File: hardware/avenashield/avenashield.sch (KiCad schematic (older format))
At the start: 4 parts, among them J3 CAN_TRA_HEADER, J4 CAN_IMP_HEADER, SW1 CAN 1 ON/OFF, SW2 CAN 2 ON/OFF

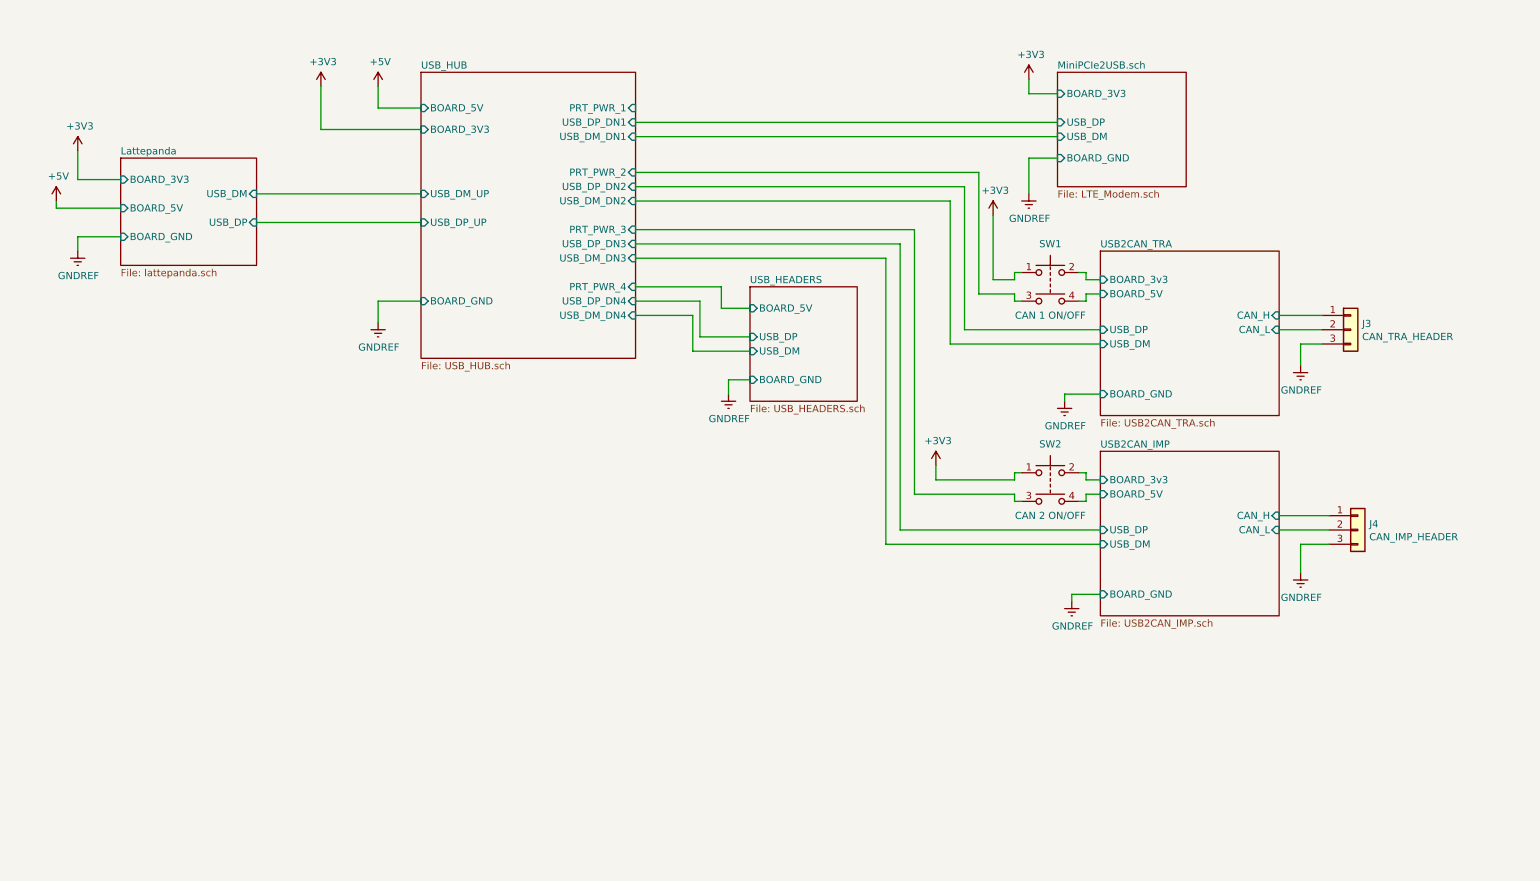
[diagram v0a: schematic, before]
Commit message: Added MiniPCIe latch clip and replaced onboard LEDs with connector
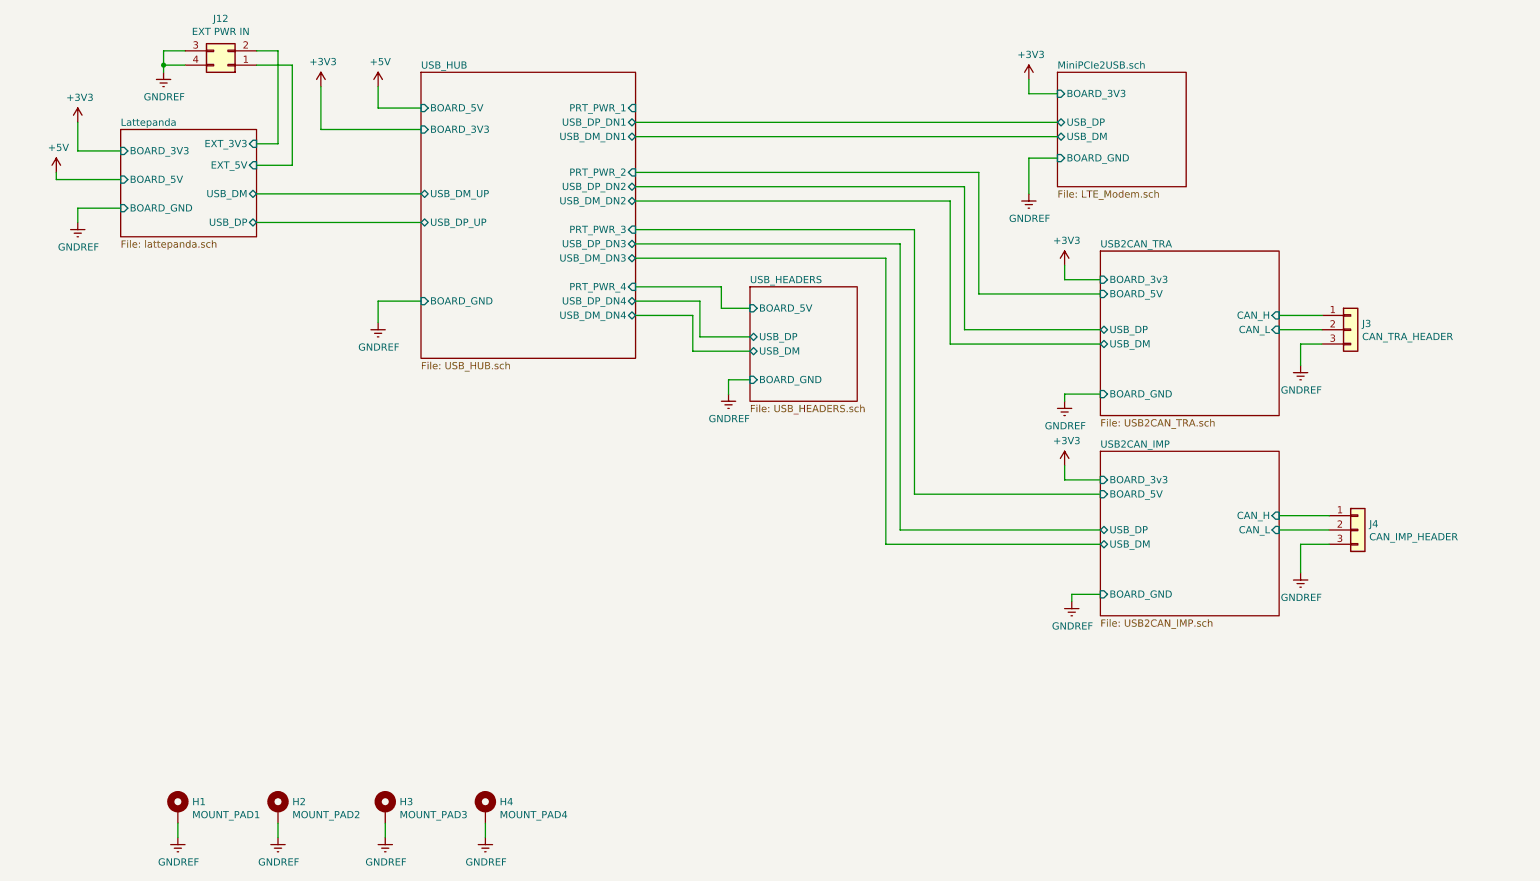
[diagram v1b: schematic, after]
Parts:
- removed SW1: CAN 1 ON/OFF, Button_Switch_SMD:SW_MEC_5GSH9, symbol Switch:SW_Push_Dual
- removed SW2: CAN 2 ON/OFF, Button_Switch_SMD:SW_MEC_5GSH9, symbol Switch:SW_Push_Dual
- added H1: MOUNT_PAD1, MountingHole:MountingHole_3.2mm_M3_Pad_Via, symbol Mechanical:MountingHole_Pad
- added H2: MOUNT_PAD2, MountingHole:MountingHole_3.2mm_M3_Pad_Via, symbol Mechanical:MountingHole_Pad
- added H3: MOUNT_PAD3, MountingHole:MountingHole_3.2mm_M3_Pad_Via, symbol Mechanical:MountingHole_Pad
- added H4: MOUNT_PAD4, MountingHole:MountingHole_3.2mm_M3_Pad_Via, symbol Mechanical:MountingHole_Pad
- added J12: EXT PWR IN, Connector_PinHeader_2.54mm:PinHeader_2x02_P2.54mm_Vertical, symbol Connector_Generic:Conn_02x02_Counter_Clockwise
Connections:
- net GNDREF: now also H1.1, H2.1, H3.1, H4.1, J12.3 (Pin_3), J12.4 (Pin_4)
- new net Lattepanda/EXT_3V3: J12.2 (Pin_2)
- new net Lattepanda/EXT_5V: J12.1 (Pin_1)

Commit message: Changed footprints for CAN connectors and replaced 3D models for headers
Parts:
- J3: footprint TerminalBlock_Phoenix:TerminalBlock_Phoenix_MKDS-1,5-3-5.08_1x03_P5.08mm_Horizontal -> TerminalBlock:TerminalBlock_bornier-3_P5.08mm; symbol Connector_Generic:Conn_01x03 -> 1546551-3:1546551-3
- J4: symbol Connector_Generic:Conn_01x03 -> 1546551-3:1546551-3
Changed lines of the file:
@@
 $EndComp
 $Comp
-L Connector_Generic:Conn_01x03 J3
+L 1546551-3:1546551-3 J3
 U 1 1 5E57F848
-P 9850 3650
-F 0 "J3" H 9930 3692 50  0000 L CNN
-F 1 "CAN_TRA_HEADER" H 9930 3601 50  0000 L CNN
-F 2 "TerminalBlock_Phoenix:TerminalBlock_Phoenix_MKDS-1,5-3-5.08_1x03_P5.08mm_Horizontal" H 9850 3650 50  0001 C CNN
-F 3 "~" H 9850 3650 50  0001 C CNN
-	1    9850 3650
+P 10050 3650
+F 0 "J3" H 10350 3700 50  0000 L CNN
+F 1 "CAN_TRA_HEADER" H 10350 3600 50  0000 L CNN
+F 2 "TerminalBlock:TerminalBlock_bornier-3_P5.08mm" H 10050 3650 50  0001 C CNN
+F 3 "~" H 10050 3650 50  0001 C CNN
+	1    10050 3650
 	1    0    0    -1
 $EndComp
 $Comp
-L Connector_Generic:Conn_01x03 J4
+L 1546551-3:1546551-3 J4
 U 1 1 5E58DC75
-P 9900 5050
-F 0 "J4" H 9980 5092 50  0000 L CNN
-F 1 "CAN_IMP_HEADER" H 9980 5001 50  0000 L CNN
-F 2 "TerminalBlock_Phoenix:TerminalBlock_Phoenix_MKDS-1,5-3-5.08_1x03_P5.08mm_Horizontal" H 9900 5050 50  0001 C CNN
-F 3 "~" H 9900 5050 50  0001 C CNN
-	1    9900 5050
+P 10100 5050
+F 0 "J4" H 10350 5100 50  0000 L CNN
+F 1 "CAN_IMP_HEADER" H 10350 5000 50  0000 L CNN
+F 2 "TerminalBlock_Phoenix:TerminalBlock_Phoenix_MKDS-1,5-3-5.08_1x03_P5.08mm_Horizontal" H 10100 5050 50  0001 C CNN
+F 3 "~" H 10100 5050 50  0001 C CNN
+	1    10100 5050
 	1    0    0    -1
 $EndComp

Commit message: Changed CAN header footprints
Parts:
- J4: footprint TerminalBlock_Phoenix:TerminalBlock_Phoenix_MKDS-1,5-3-5.08_1x03_P5.08mm_Horizontal -> TerminalBlock_Phoenix:TerminalBlock_Phoenix_PT-1,5-3-3.5-H_1x03_P3.50mm_Horizontal
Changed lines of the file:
@@
 F 0 "J4" H 10350 5100 50  0000 L CNN
 F 1 "CAN_IMP_HEADER" H 10350 5000 50  0000 L CNN
-F 2 "TerminalBlock_Phoenix:TerminalBlock_Phoenix_MKDS-1,5-3-5.08_1x03_P5.08mm_Horizontal" H 10100 5050 50  0001 C CNN
+F 2 "TerminalBlock_Phoenix:TerminalBlock_Phoenix_PT-1,5-3-3.5-H_1x03_P3.50mm_Horizontal" H 10100 5050 50  0001 C CNN
 F 3 "~" H 10100 5050 50  0001 C CNN
 	1    10100 5050

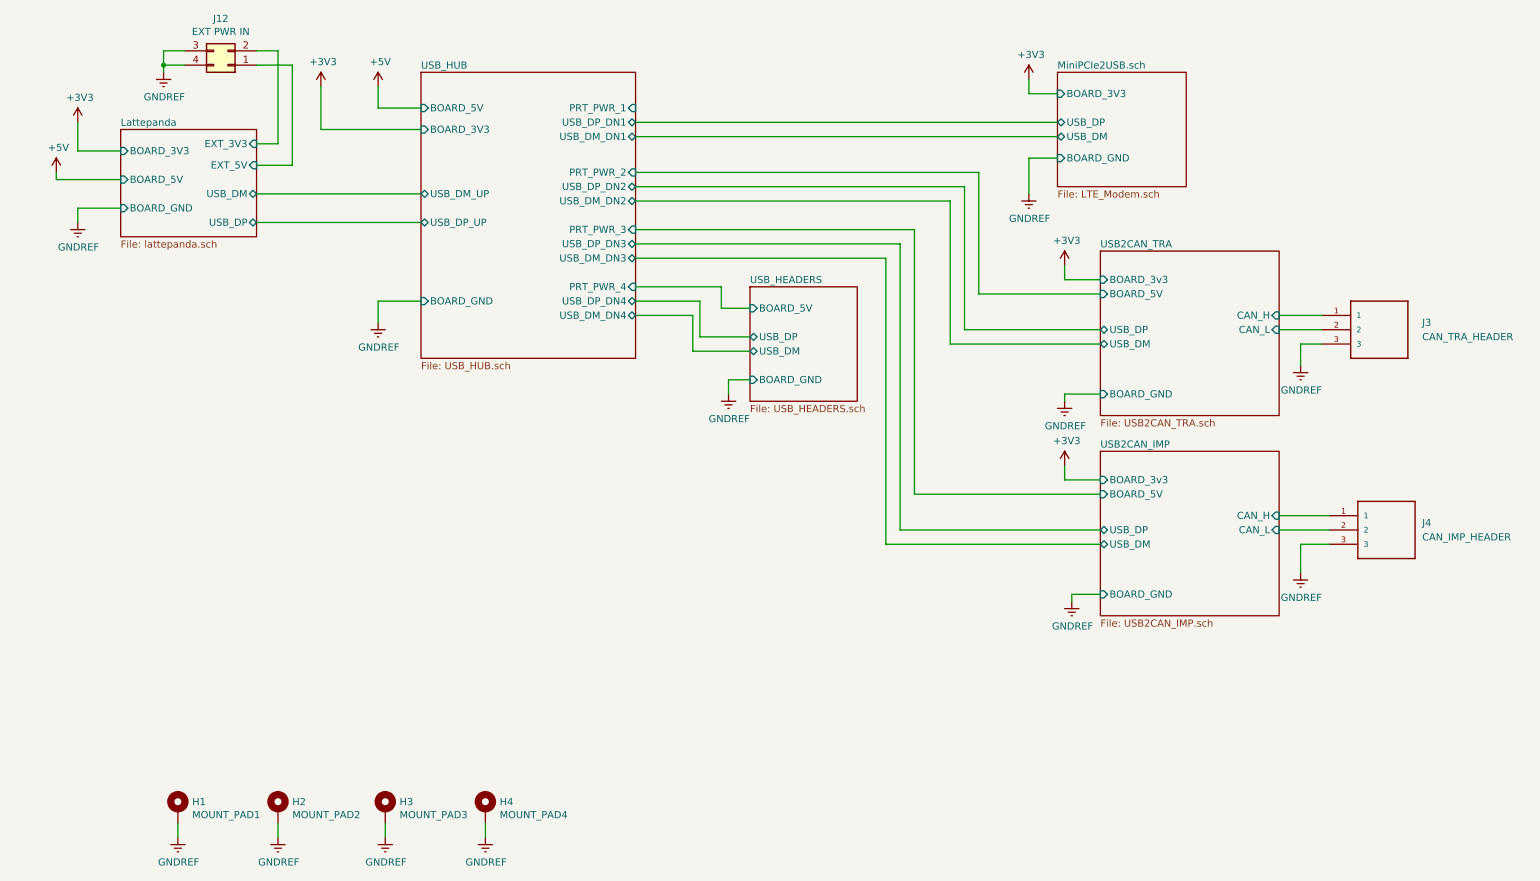
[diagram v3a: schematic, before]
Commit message: Improved I2C bus routing
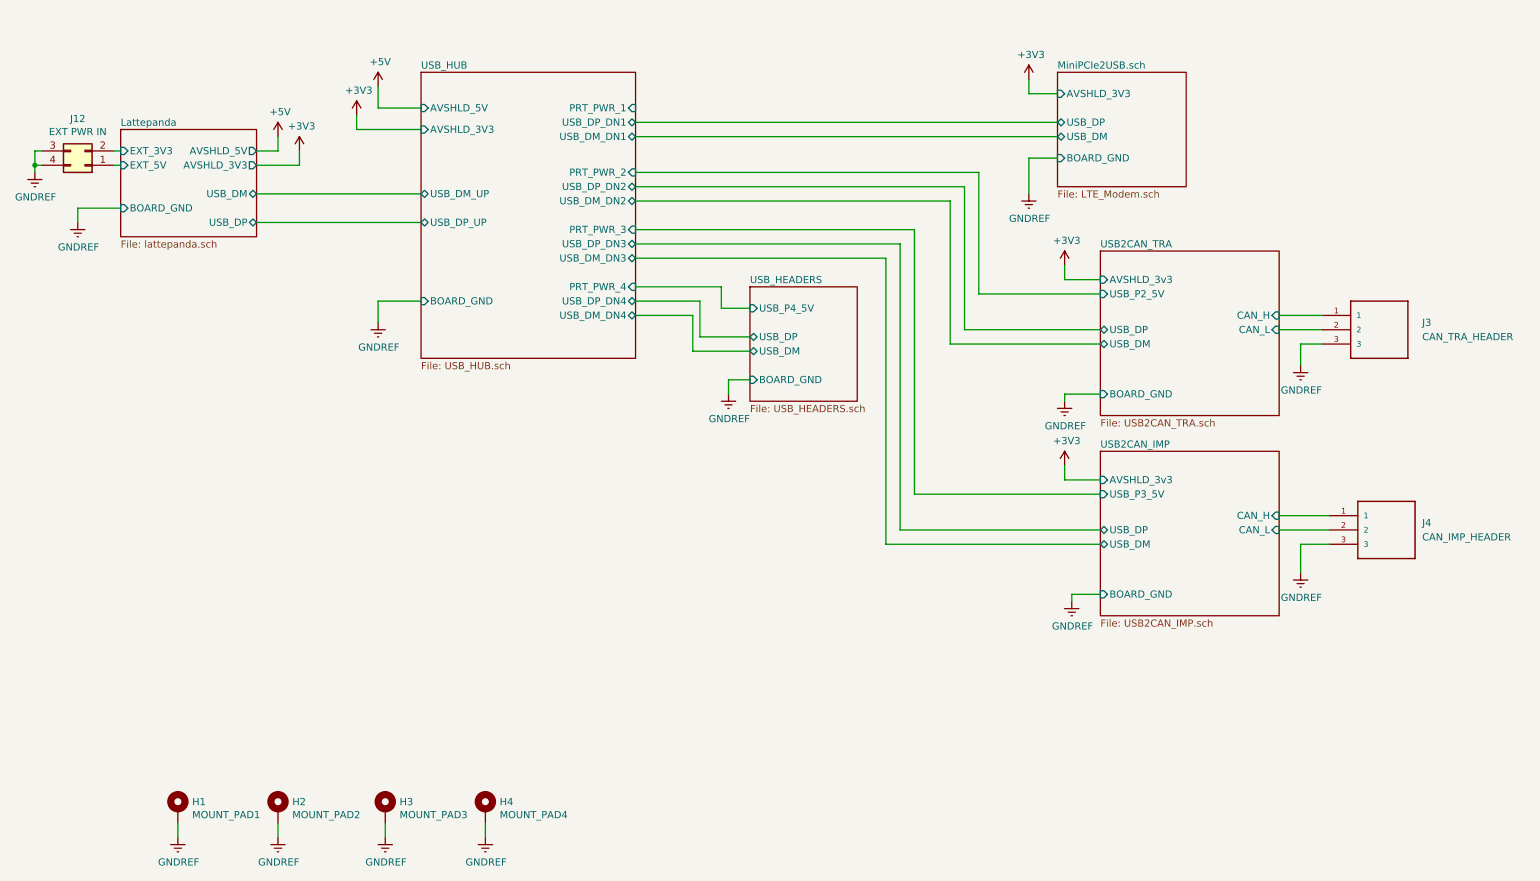
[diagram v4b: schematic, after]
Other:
- moved on the sheet: J12
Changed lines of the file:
@@
 Comment4 ""
 $EndDescr
-Connection ~ 1550 1800
-Wire Wire Line
-	800  2600 800  2550
-Wire Wire Line
-	950  2200 950  2400
-Wire Wire Line
-	950  2400 1250 2400
 Wire Wire Line
 	950  2800 1250 2800
@@
 	950  2900 950  2800
 Wire Wire Line
-	1250 2600 800  2600
-Wire Wire Line
-	1550 1700 1700 1700
-Wire Wire Line
-	1550 1800 1550 1700
-Wire Wire Line
-	1550 1850 1550 1800
-Wire Wire Line
-	1700 1800 1550 1800
-Wire Wire Line
-	2200 1700 2350 1700
-Wire Wire Line
-	2200 1800 2450 1800
-Wire Wire Line
 	2200 2900 3350 2900
 Wire Wire Line
-	2350 1700 2350 2350
-Wire Wire Line
-	2350 2350 2200 2350
-Wire Wire Line
-	2450 1800 2450 2500
-Wire Wire Line
-	2450 2500 2200 2500
-Wire Wire Line
-	2650 2250 2650 1950
-Wire Wire Line
 	3050 1950 3050 2100
 Wire Wire Line
@@
 Wire Wire Line
 	3050 3600 3050 3450
-Wire Wire Line
-	3350 2250 2650 2250
 Wire Wire Line
 	3350 2700 2200 2700
@@
 L power:+5V #PWR0124
 U 1 1 5E4DA317
-P 800 2550
-F 0 "#PWR0124" H 800 2400 50  0001 C CNN
-F 1 "+5V" H 815 2723 50  0000 C CNN
-F 2 "" H 800 2550 50  0001 C CNN
-F 3 "" H 800 2550 50  0001 C CNN
-	1    800  2550
+P 2350 2300
+F 0 "#PWR0124" H 2350 2150 50  0001 C CNN
+F 1 "+5V" H 2365 2473 50  0000 C CNN
+F 2 "" H 2350 2300 50  0001 C CNN
+F 3 "" H 2350 2300 50  0001 C CNN
+	1    2350 2300
 	1    0    0    -1
 $EndComp
@@
 L power:+3V3 #PWR0123
 U 1 1 5E4DA00F
-P 950 2200
-F 0 "#PWR0123" H 950 2050 50  0001 C CNN
-F 1 "+3V3" H 965 2373 50  0000 C CNN
-F 2 "" H 950 2200 50  0001 C CNN
-F 3 "" H 950 2200 50  0001 C CNN
-	1    950  2200
+P 2500 2400
+F 0 "#PWR0123" H 2500 2250 50  0001 C CNN
+F 1 "+3V3" H 2515 2573 50  0000 C CNN
+F 2 "" H 2500 2400 50  0001 C CNN
+F 3 "" H 2500 2400 50  0001 C CNN
+	1    2500 2400
 	1    0    0    -1
 $EndComp
@@
 L power:+3V3 #PWR0126
 U 1 1 5E4DCB6D
-P 2650 1950
-F 0 "#PWR0126" H 2650 1800 50  0001 C CNN
-F 1 "+3V3" H 2665 2123 50  0000 C CNN
-F 2 "" H 2650 1950 50  0001 C CNN
-F 3 "" H 2650 1950 50  0001 C CNN
-	1    2650 1950
+P 2900 2150
+F 0 "#PWR0126" H 2900 2000 50  0001 C CNN
+F 1 "+3V3" H 2915 2323 50  0000 C CNN
+F 2 "" H 2900 2150 50  0001 C CNN
+F 3 "" H 2900 2150 50  0001 C CNN
+	1    2900 2150
 	1    0    0    -1
 $EndComp
@@
 L power:GNDREF #PWR0196
 U 1 1 5E7AC789
-P 1550 1850
-F 0 "#PWR0196" H 1550 1600 50  0001 C CNN
-F 1 "GNDREF" H 1555 1677 50  0000 C CNN
-F 2 "" H 1550 1850 50  0001 C CNN
-F 3 "" H 1550 1850 50  0001 C CNN
-	1    1550 1850
+P 650 2550
+F 0 "#PWR0196" H 650 2300 50  0001 C CNN
+F 1 "GNDREF" H 655 2377 50  0000 C CNN
+F 2 "" H 650 2550 50  0001 C CNN
+F 3 "" H 650 2550 50  0001 C CNN
+	1    650  2550
 	1    0    0    -1
 $EndComp
@@
 L Connector_Generic:Conn_02x02_Counter_Clockwise J12
 U 1 1 5E7A4A4E
-P 2000 1800
-F 0 "J12" H 2050 1475 50  0000 C CNN
-F 1 "EXT PWR IN" H 2050 1566 50  0000 C CNN
-F 2 "Connector_PinHeader_2.54mm:PinHeader_2x02_P2.54mm_Vertical" H 2000 1800 50  0001 C CNN
-F 3 "~" H 2000 1800 50  0001 C CNN
-	1    2000 1800
+P 1000 2500
+F 0 "J12" H 1050 2175 50  0000 C CNN
+F 1 "EXT PWR IN" H 1050 2266 50  0000 C CNN
+F 2 "Connector_PinHeader_2.54mm:PinHeader_2x02_P2.54mm_Vertical" H 1000 2500 50  0001 C CNN
+F 3 "~" H 1000 2500 50  0001 C CNN
+	1    1000 2500
 	-1   0    0    1
 $EndComp
@@
 F0 "MiniPCIe2USB.sch" 50
 F1 "LTE_Modem.sch" 50
-F2 "BOARD_3V3" I L 7800 2000 50
+F2 "AVSHLD_3V3" I L 7800 2000 50
 F3 "USB_DP" B L 7800 2200 50
 F4 "USB_DM" B L 7800 2300 50
@@
 F4 "CAN_H" I R 9350 4950 50
 F5 "CAN_L" I R 9350 5050 50
-F6 "BOARD_3v3" I L 8100 4700 50
-F7 "BOARD_5V" I L 8100 4800 50
+F6 "AVSHLD_3v3" I L 8100 4700 50
+F7 "USB_P3_5V" I L 8100 4800 50
 F8 "BOARD_GND" I L 8100 5500 50
 $EndSheet
@@
 F4 "CAN_H" I R 9350 3550 50
 F5 "CAN_L" I R 9350 3650 50
-F6 "BOARD_3v3" I L 8100 3300 50
-F7 "BOARD_5V" I L 8100 3400 50
+F6 "AVSHLD_3v3" I L 8100 3300 50
+F7 "USB_P2_5V" I L 8100 3400 50
 F8 "BOARD_GND" I L 8100 4100 50
 $EndSheet
@@
 F2 "USB_DM" B L 5650 3800 50
 F3 "USB_DP" B L 5650 3700 50
-F4 "BOARD_5V" I L 5650 3500 50
+F4 "USB_P4_5V" I L 5650 3500 50
 F5 "BOARD_GND" I L 5650 4000 50
 $EndSheet
@@
 F12 "PRT_PWR_3" I R 4850 2950 50
 F13 "PRT_PWR_4" I R 4850 3350 50
-F14 "BOARD_5V" I L 3350 2100 50
-F15 "BOARD_3V3" I L 3350 2250 50
+F14 "AVSHLD_5V" I L 3350 2100 50
+F15 "AVSHLD_3V3" I L 3350 2250 50
 F16 "BOARD_GND" I L 3350 3450 50
 F17 "USB_DP_UP" B L 3350 2900 50
@@
 F2 "USB_DM" B R 2200 2700 50
 F3 "USB_DP" B R 2200 2900 50
-F4 "BOARD_3V3" I L 1250 2400 50
-F5 "BOARD_5V" I L 1250 2600 50
+F4 "AVSHLD_3V3" O R 2200 2500 50
+F5 "AVSHLD_5V" O R 2200 2400 50
 F6 "BOARD_GND" I L 1250 2800 50
-F7 "EXT_3V3" I R 2200 2350 50
-F8 "EXT_5V" I R 2200 2500 50
+F7 "EXT_3V3" I L 1250 2400 50
+F8 "EXT_5V" I L 1250 2500 50
 $EndSheet
+Wire Wire Line
+	2200 2400 2350 2400
+Wire Wire Line
+	2350 2400 2350 2300
+Wire Wire Line
+	2200 2500 2500 2500
+Wire Wire Line
+	2500 2500 2500 2400
+Wire Wire Line
+	650  2550 650  2500
+Wire Wire Line
+	650  2500 700  2500
+Wire Wire Line
+	650  2500 650  2400
+Wire Wire Line
+	650  2400 700  2400
+Connection ~ 650  2500
+Wire Wire Line
+	2900 2150 2900 2250
+Wire Wire Line
+	2900 2250 3350 2250
+Wire Wire Line
+	1200 2400 1250 2400
+Wire Wire Line
+	1200 2500 1250 2500
 $EndSCHEMATC
